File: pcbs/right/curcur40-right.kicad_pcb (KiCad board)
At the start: 2 copper layers, 124.3 x 91.8 mm, 88 parts, among them U1 PMW3360DM-T2QU, U2 TLV74318PDBVR

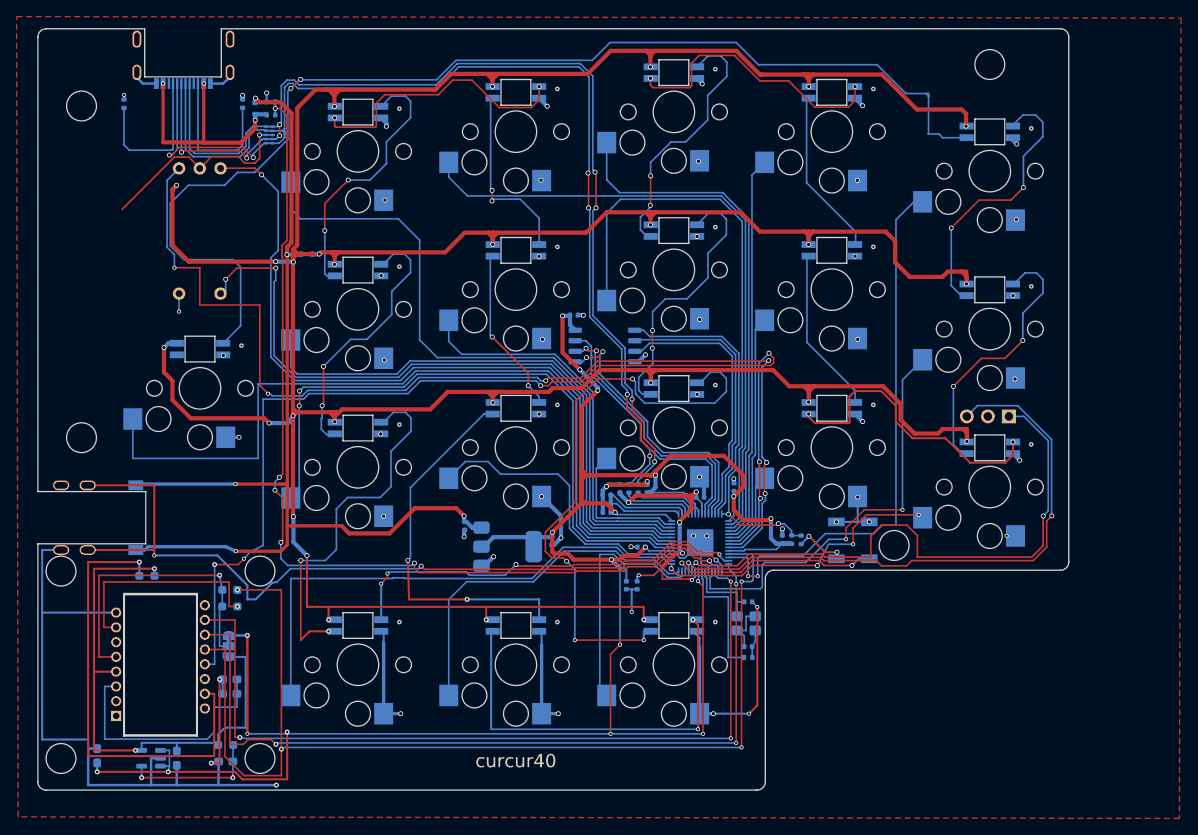
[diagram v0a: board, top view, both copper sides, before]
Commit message: fix(pcb): update spacer holes to 3.25mm, shift SMDSW1/2, remove 0.4mm NPTH hole, and sync U1/CKW12 attributes
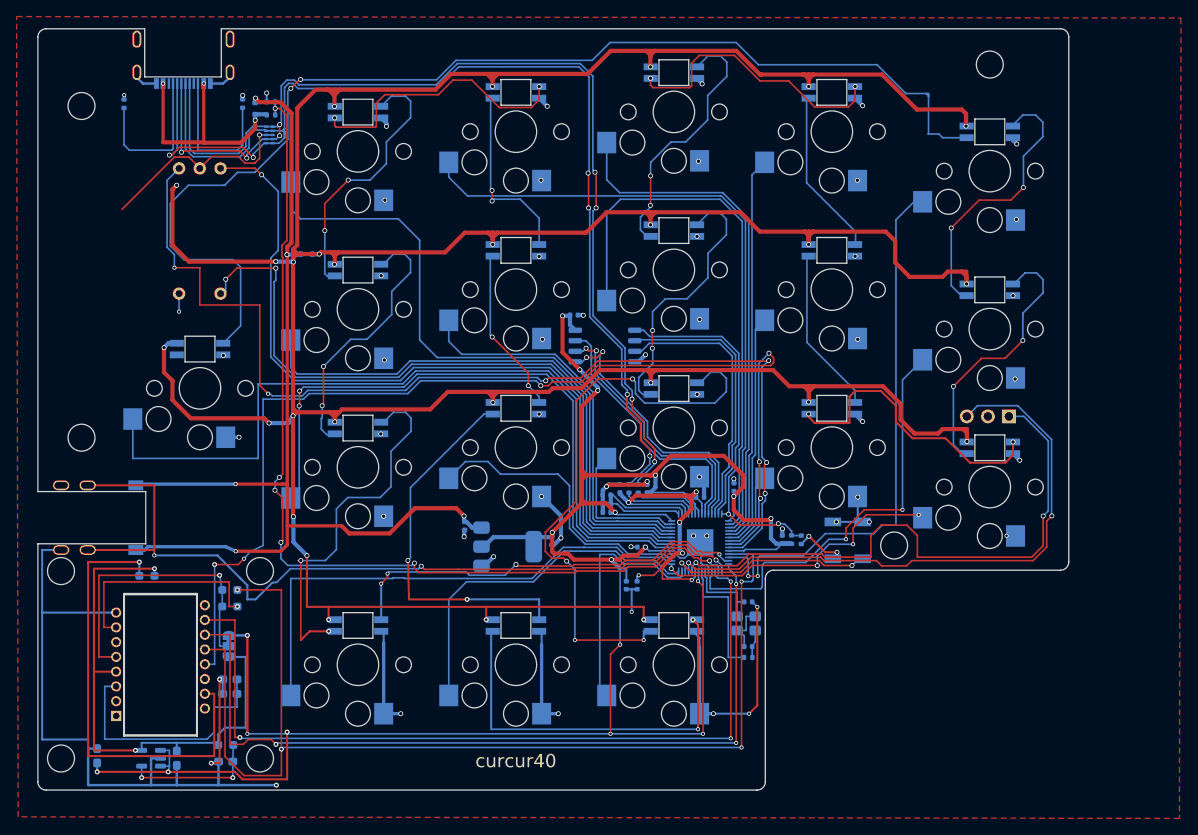
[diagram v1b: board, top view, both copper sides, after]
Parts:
- moved rSMDSW2 0.80 mm to (94.2, 37.4)
- moved rSMDSW1 0.44 mm to (90.6, 37.4)
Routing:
- net Net-(rU1-RUN): track 25.4 -> 24.6 mm
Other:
- outline, holes or cut-outs redrawn
